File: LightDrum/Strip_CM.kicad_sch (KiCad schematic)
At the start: 26 parts, among them T701 NET-TIE, T702 NET-TIE, T703 NET-TIE, T704 NET-TIE, T705 NET-TIE, T706 NET-TIE, T707 NET-TIE, T708 NET-TIE, T709 NET-TIE, T710 NET-TIE, T711 NET-TIE, T712 NET-TIE, T713 NET-TIE, T714 NET-TIE, T715 NET-TIE, T716 NET-TIE, U701 INA4181 A2, U702 INA4181 A2

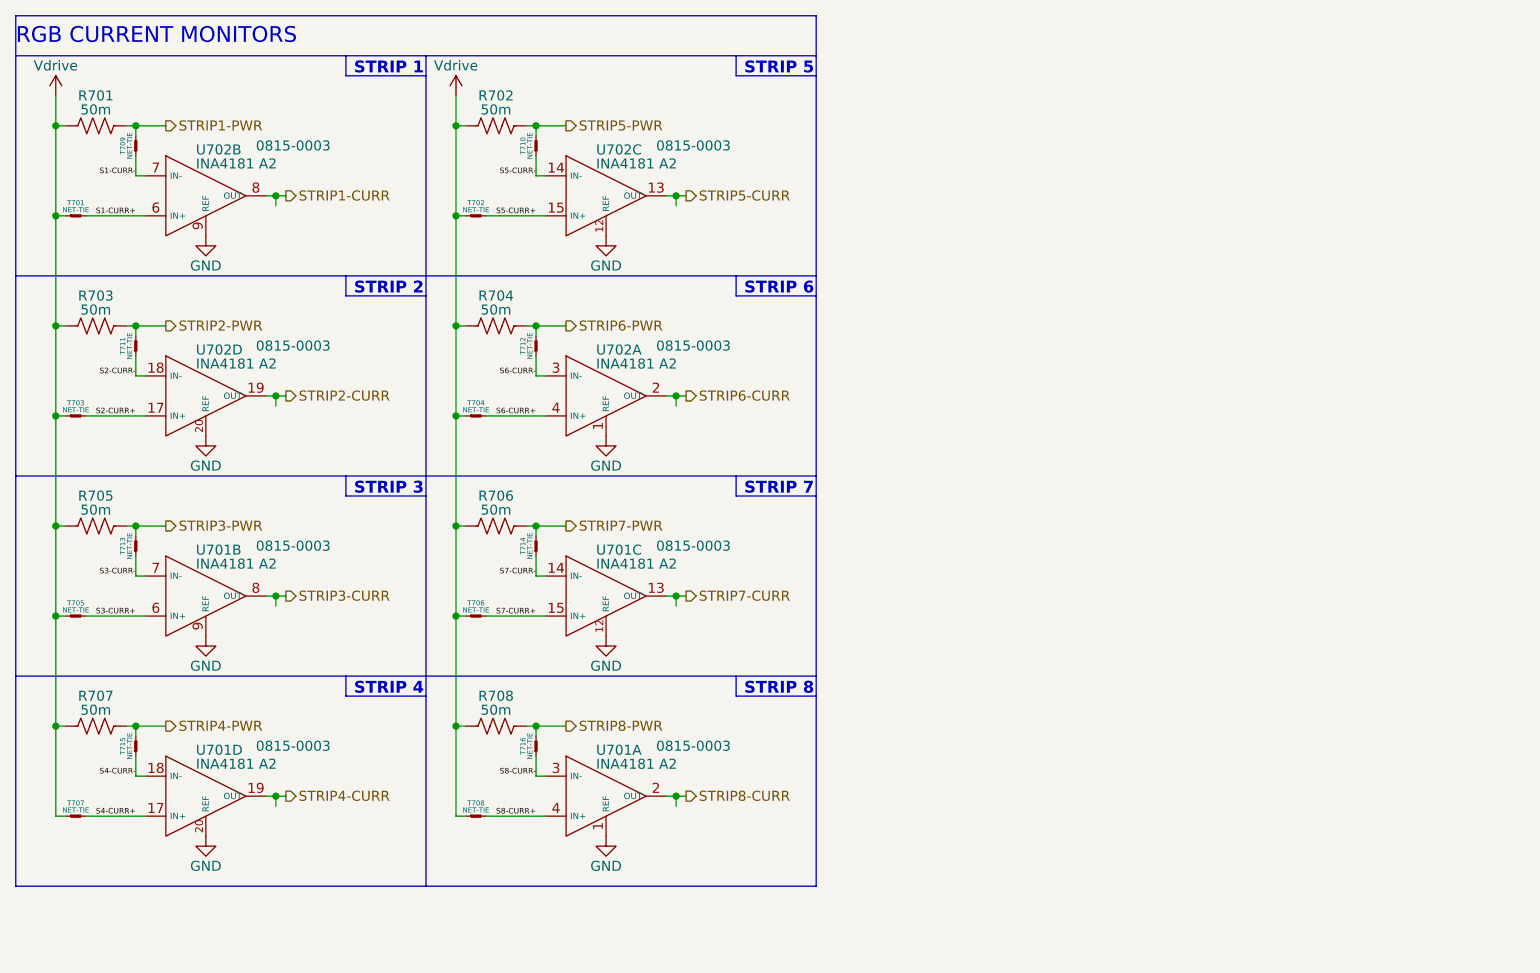
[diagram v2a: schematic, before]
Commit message: Component placement complete
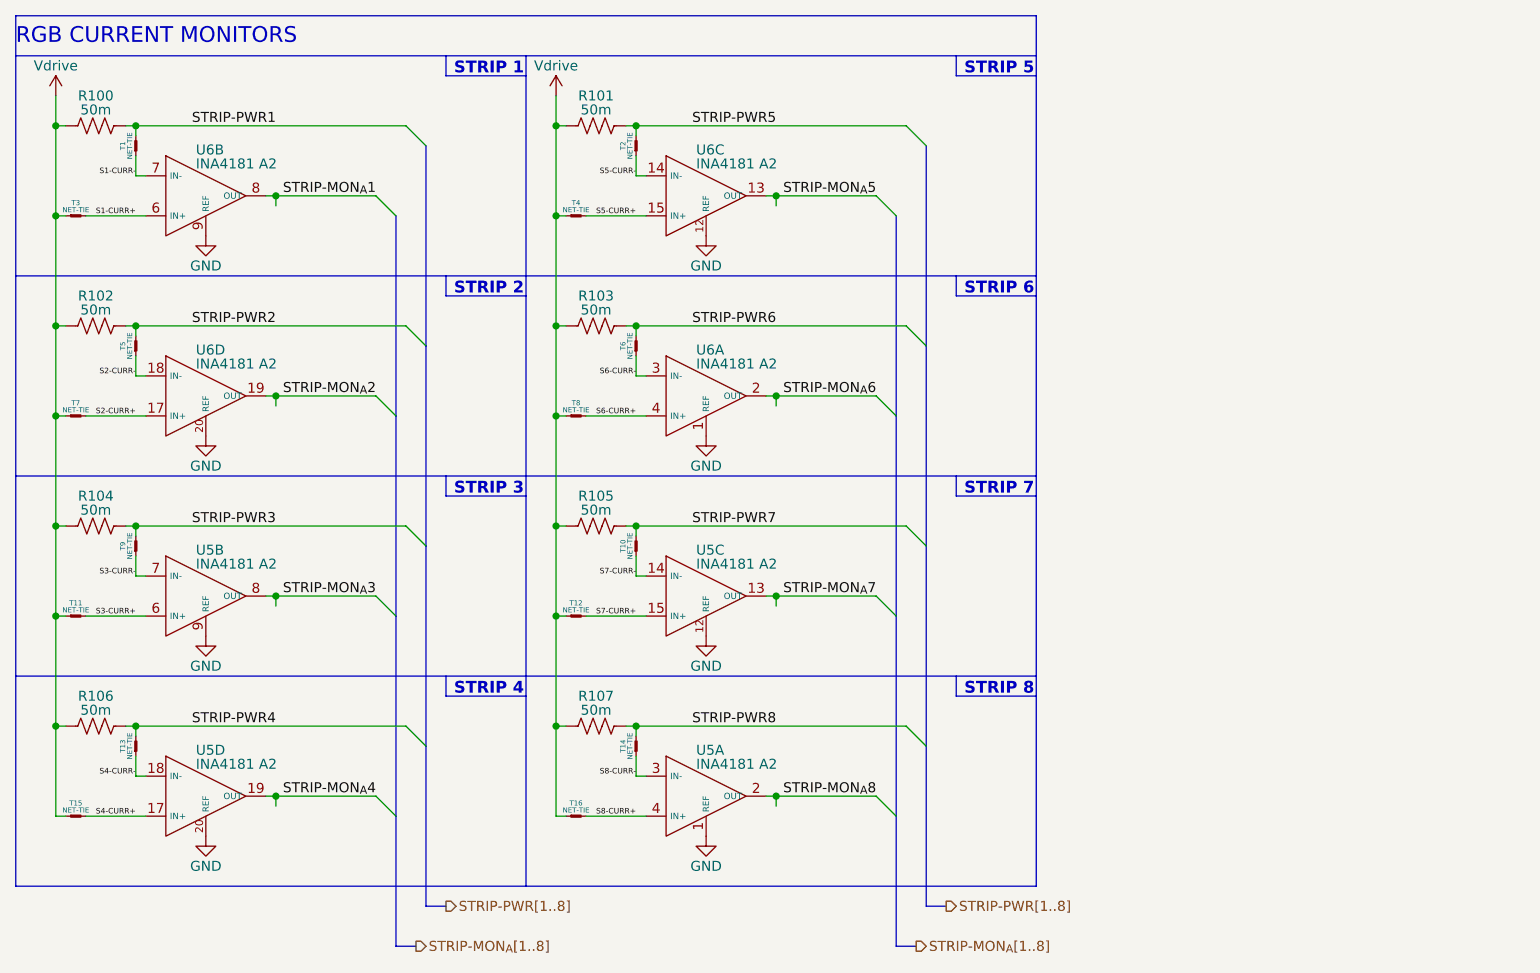
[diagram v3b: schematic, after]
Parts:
- renumbered R701 to R100, R702 to R101, R703 to R102, R704 to R103, R705 to R104, R706 to R105, R707 to R106, R708 to R107, T709 to T1, T714 to T10, T705 to T11, T706 to T12, T715 to T13, T716 to T14, T707 to T15, T708 to T16, T710 to T2, T701 to T3, T702 to T4, T711 to T5, T712 to T6, T703 to T7, T704 to T8, T713 to T9, U701 to U5, U702 to U6
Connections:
- net STRIP1-CURR renamed STRIP-MON_{A}1
- net STRIP1-PWR renamed STRIP-PWR1
- net STRIP2-CURR renamed STRIP-MON_{A}2
- net STRIP2-PWR renamed STRIP-PWR2
- net STRIP3-CURR renamed STRIP-MON_{A}3
- net STRIP3-PWR renamed STRIP-PWR3
- net STRIP4-CURR renamed STRIP-MON_{A}4
- net STRIP4-PWR renamed STRIP-PWR4
- net STRIP5-CURR renamed STRIP-MON_{A}5
- net STRIP5-PWR renamed STRIP-PWR5
- net STRIP6-CURR renamed STRIP-MON_{A}6
- net STRIP6-PWR renamed STRIP-PWR6
- net STRIP7-CURR renamed STRIP-MON_{A}7
- net STRIP7-PWR renamed STRIP-PWR7
- net STRIP8-CURR renamed STRIP-MON_{A}8
- net STRIP8-PWR renamed STRIP-PWR8
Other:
- moved on the sheet: R101, R103, R105, R107, T10, T12, T14, T16, T2, T4, T6, T8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

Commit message: First draft layout almost complete
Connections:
- net S1-CURR+: now also U6.15 (IN+); no longer U6.6 (IN+)
- net S1-CURR-: now also U6.14 (IN-); no longer U6.7 (IN-)
- net S2-CURR+: now also U6.4 (IN+); no longer U6.17 (IN+)
- net S2-CURR-: now also U6.3 (IN-); no longer U6.18 (IN-)
- net S3-CURR+: now also U5.15 (IN+); no longer U5.6 (IN+)
- net S3-CURR-: now also U5.14 (IN-); no longer U5.7 (IN-)
- net S4-CURR+: now also U5.4 (IN+); no longer U5.17 (IN+)
- net S4-CURR-: now also U5.3 (IN-); no longer U5.18 (IN-)
- net S5-CURR+: now also U6.17 (IN+); no longer U6.15 (IN+)
- net S5-CURR-: now also U6.18 (IN-); no longer U6.14 (IN-)
- net S6-CURR+: now also U6.6 (IN+); no longer U6.4 (IN+)
- net S6-CURR-: now also U6.7 (IN-); no longer U6.3 (IN-)
- net S7-CURR+: now also U5.17 (IN+); no longer U5.15 (IN+)
- net S7-CURR-: now also U5.18 (IN-); no longer U5.14 (IN-)
- net S8-CURR+: now also U5.6 (IN+); no longer U5.4 (IN+)
- net S8-CURR-: now also U5.7 (IN-); no longer U5.3 (IN-)
- net STRIP-MON_{A}1: now also U6.13 (OUT); no longer U6.8 (OUT)
- net STRIP-MON_{A}2: now also U6.2 (OUT); no longer U6.19 (OUT)
- net STRIP-MON_{A}3: now also U5.13 (OUT); no longer U5.8 (OUT)
- net STRIP-MON_{A}4: now also U5.2 (OUT); no longer U5.19 (OUT)
- net STRIP-MON_{A}5: now also U6.19 (OUT); no longer U6.13 (OUT)
- net STRIP-MON_{A}6: now also U6.8 (OUT); no longer U6.2 (OUT)
- net STRIP-MON_{A}7: now also U5.19 (OUT); no longer U5.13 (OUT)
- net STRIP-MON_{A}8: now also U5.8 (OUT); no longer U5.2 (OUT)
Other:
- moved on the sheet: U5A, U5B, U5C, U5D, U6A, U6B, U6C, U6D

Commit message: PCB Lock REV11
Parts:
- T1, T10, T11, T12, T13, T14, T15, T16, T2, T3, T4, T5, T6, T7, T8, T9: footprint Daxxn_Other:NetTie-2_SMD_Pad0.25mm -> Daxxn_Other:NetTie-2-SMALL_SMD_Pad0.2mm
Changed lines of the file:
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@@
       (effects (font (size 0.64 0.64)))
     )
-    (property "Footprint" "Daxxn_Other:NetTie-2_SMD_Pad0.25mm" (at 91.44 41.91 0)
+    (property "Footprint" "Daxxn_Other:NetTie-2-SMALL_SMD_Pad0.2mm" (at 91.44 41.91 0)
       (effects (font (size 1.27 1.27)) hide)
     )
@@
       (effects (font (size 0.64 0.64)))
     )
-    (property "Footprint" "Daxxn_Other:NetTie-2_SMD_Pad0.25mm" (at 15.24 88.9 0)
+    (property "Footprint" "Daxxn_Other:NetTie-2-SMALL_SMD_Pad0.2mm" (at 15.24 88.9 0)
       (effects (font (size 1.27 1.27)) hide)
     )
@@
       (effects (font (size 0.64 0.64)))
     )
-    (property "Footprint" "Daxxn_Other:NetTie-2_SMD_Pad0.25mm" (at 78.74 38.1 0)
+    (property "Footprint" "Daxxn_Other:NetTie-2-SMALL_SMD_Pad0.2mm" (at 78.74 38.1 0)
       (effects (font (size 1.27 1.27)) hide)
     )
@@
       (effects (font (size 0.64 0.64)))
     )
-    (property "Footprint" "Daxxn_Other:NetTie-2_SMD_Pad0.25mm" (at 27.94 92.71 0)
+    (property "Footprint" "Daxxn_Other:NetTie-2-SMALL_SMD_Pad0.2mm" (at 27.94 92.71 0)
       (effects (font (size 1.27 1.27)) hide)
     )
@@
       (effects (font (size 0.64 0.64)))
     )
-    (property "Footprint" "Daxxn_Other:NetTie-2_SMD_Pad0.25mm" (at 15.24 38.1 0)
+    (property "Footprint" "Daxxn_Other:NetTie-2-SMALL_SMD_Pad0.2mm" (at 15.24 38.1 0)
       (effects (font (size 1.27 1.27)) hide)
     )
@@
       (effects (font (size 0.64 0.64)))
     )
-    (property "Footprint" "Daxxn_Other:NetTie-2_SMD_Pad0.25mm" (at 78.74 88.9 0)
+    (property "Footprint" "Daxxn_Other:NetTie-2-SMALL_SMD_Pad0.2mm" (at 78.74 88.9 0)
       (effects (font (size 1.27 1.27)) hide)
     )
@@
       (effects (font (size 0.64 0.64)))
     )
-    (property "Footprint" "Daxxn_Other:NetTie-2_SMD_Pad0.25mm" (at 91.44 67.31 0)
+    (property "Footprint" "Daxxn_Other:NetTie-2-SMALL_SMD_Pad0.2mm" (at 91.44 67.31 0)
       (effects (font (size 1.27 1.27)) hide)
     )
@@
       (effects (font (size 0.64 0.64)))
     )
-    (property "Footprint" "Daxxn_Other:NetTie-2_SMD_Pad0.25mm" (at 78.74 114.3 0)
+    (property "Footprint" "Daxxn_Other:NetTie-2-SMALL_SMD_Pad0.2mm" (at 78.74 114.3 0)
       (effects (font (size 1.27 1.27)) hide)
     )
@@
       (effects (font (size 0.64 0.64)))
     )
-    (property "Footprint" "Daxxn_Other:NetTie-2_SMD_Pad0.25mm" (at 27.94 118.11 0)
+    (property "Footprint" "Daxxn_Other:NetTie-2-SMALL_SMD_Pad0.2mm" (at 27.94 118.11 0)
       (effects (font (size 1.27 1.27)) hide)
     )
@@
       (effects (font (size 0.64 0.64)))
     )
-    (property "Footprint" "Daxxn_Other:NetTie-2_SMD_Pad0.25mm" (at 91.44 92.71 0)
+    (property "Footprint" "Daxxn_Other:NetTie-2-SMALL_SMD_Pad0.2mm" (at 91.44 92.71 0)
       (effects (font (size 1.27 1.27)) hide)
     )
@@
       (effects (font (size 0.64 0.64)))
     )
-    (property "Footprint" "Daxxn_Other:NetTie-2_SMD_Pad0.25mm" (at 78.74 63.5 0)
+    (property "Footprint" "Daxxn_Other:NetTie-2-SMALL_SMD_Pad0.2mm" (at 78.74 63.5 0)
       (effects (font (size 1.27 1.27)) hide)
     )
@@
       (effects (font (size 0.64 0.64)))
     )
-    (property "Footprint" "Daxxn_Other:NetTie-2_SMD_Pad0.25mm" (at 27.94 41.91 0)
+    (property "Footprint" "Daxxn_Other:NetTie-2-SMALL_SMD_Pad0.2mm" (at 27.94 41.91 0)
       (effects (font (size 1.27 1.27)) hide)
     )
@@
       (effects (font (size 0.64 0.64)))
     )
-    (property "Footprint" "Daxxn_Other:NetTie-2_SMD_Pad0.25mm" (at 91.44 118.11 0)
+    (property "Footprint" "Daxxn_Other:NetTie-2-SMALL_SMD_Pad0.2mm" (at 91.44 118.11 0)
       (effects (font (size 1.27 1.27)) hide)
     )
@@
       (effects (font (size 0.64 0.64)))
     )
-    (property "Footprint" "Daxxn_Other:NetTie-2_SMD_Pad0.25mm" (at 15.24 114.3 0)
+    (property "Footprint" "Daxxn_Other:NetTie-2-SMALL_SMD_Pad0.2mm" (at 15.24 114.3 0)
       (effects (font (size 1.27 1.27)) hide)
     )
@@
       (effects (font (size 0.64 0.64)))
     )
-    (property "Footprint" "Daxxn_Other:NetTie-2_SMD_Pad0.25mm" (at 27.94 67.31 0)
+    (property "Footprint" "Daxxn_Other:NetTie-2-SMALL_SMD_Pad0.2mm" (at 27.94 67.31 0)
       (effects (font (size 1.27 1.27)) hide)
     )
@@
       (effects (font (size 0.64 0.64)))
     )
-    (property "Footprint" "Daxxn_Other:NetTie-2_SMD_Pad0.25mm" (at 15.24 63.5 0)
-      (effects (font (size 1.27 1.27)) hide)
-    )
+    (property "Footprint" "Daxxn_Other:NetTie-2-SMALL_SMD_Pad0.2mm" (at 15.24 63.5 0)
+      (effects (font (size 1.27 1.27)) hide)
+    )

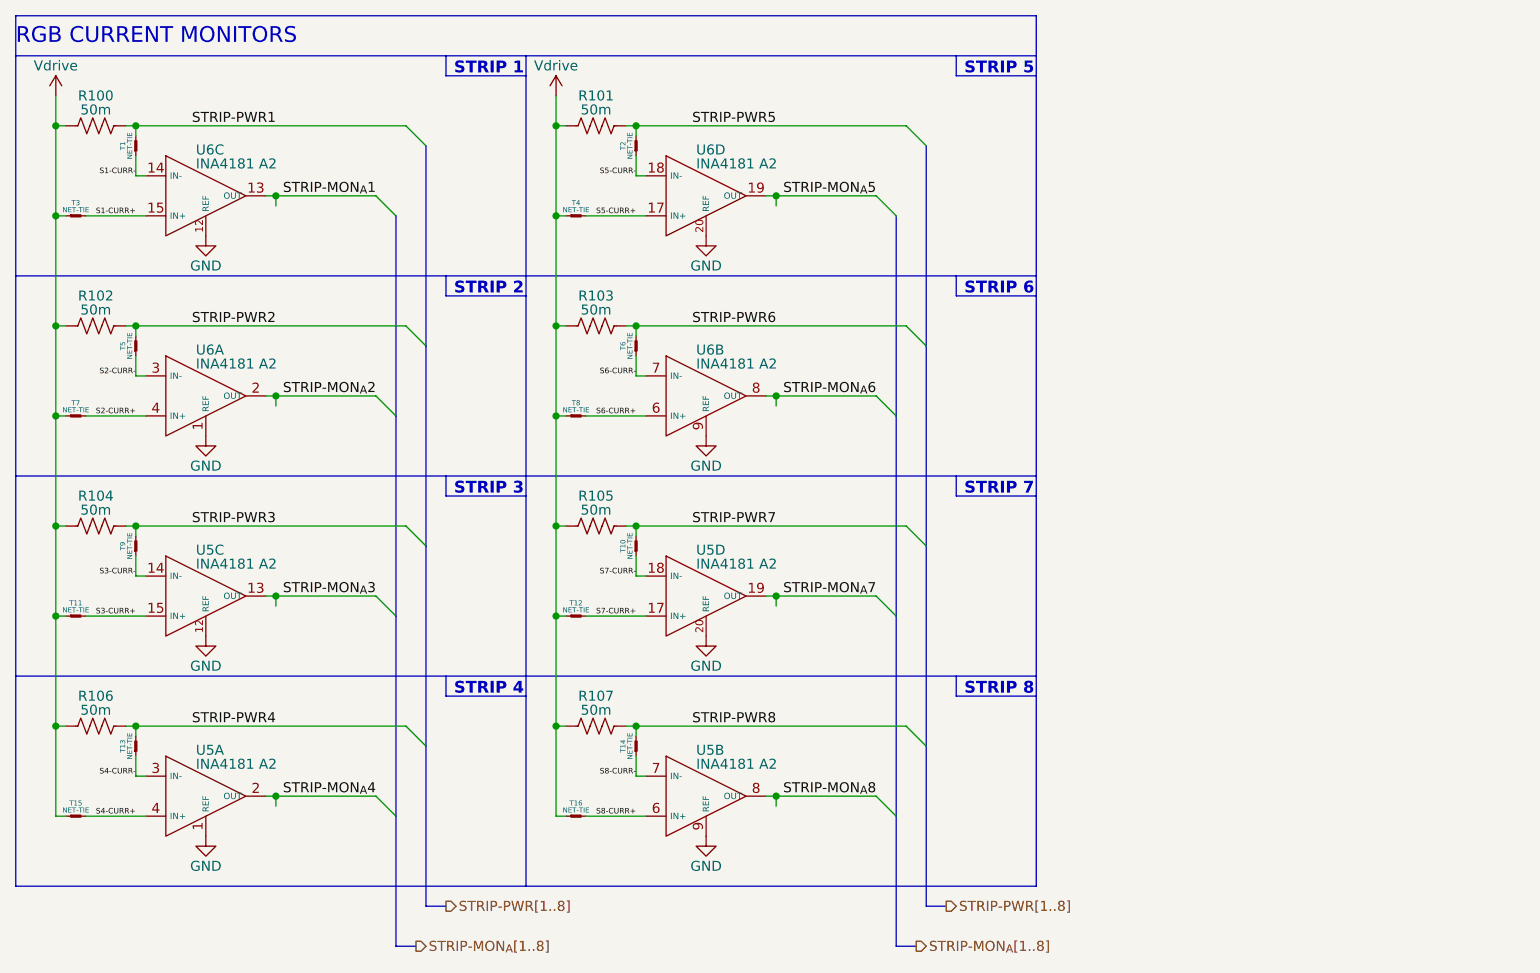
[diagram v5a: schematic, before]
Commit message: Replace DSub with much better ECU conn
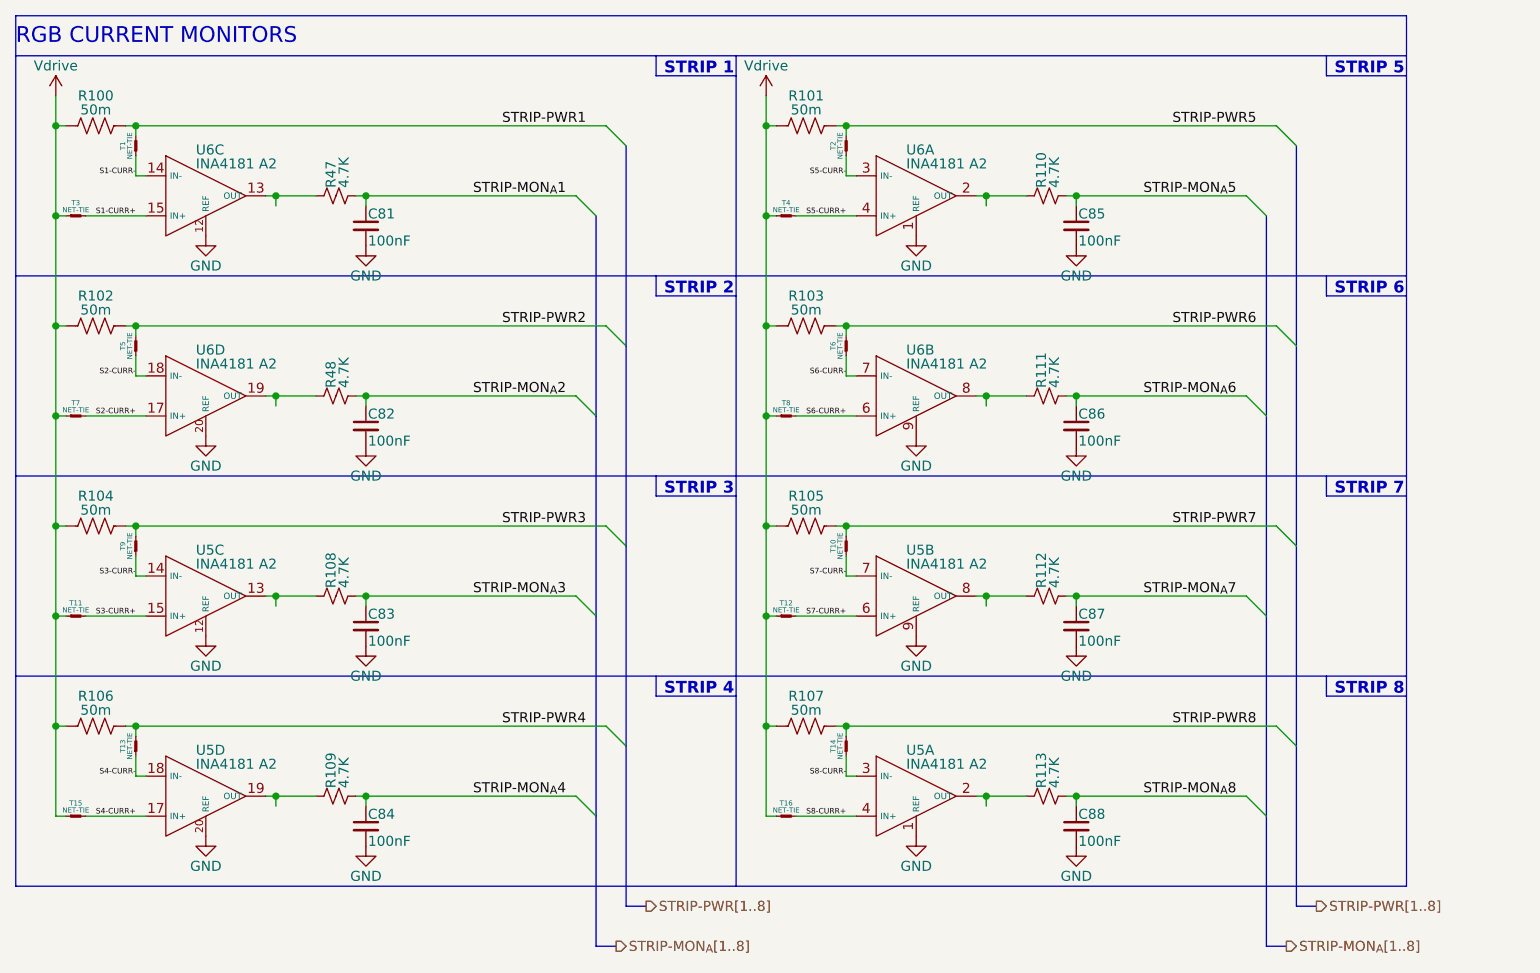
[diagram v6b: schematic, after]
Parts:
- added C81, C82, C83, C84, C85, C86, C87, C88: 100nF, Capacitor_SMD:C_0402_1005Metric, symbol Daxxn_Device:C
- added R108, R109, R110, R111, R112, R113, R47, R48: 4.7K, Resistor_SMD:R_0402_1005Metric, symbol Daxxn_Device:R
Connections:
- net GND: now also C81.2, C82.2, C83.2, C84.2, C85.2, C86.2, C87.2, C88.2
- net S2-CURR+: now also U6.17 (IN+); no longer U6.4 (IN+)
- net S2-CURR-: now also U6.18 (IN-); no longer U6.3 (IN-)
- net S4-CURR+: now also U5.17 (IN+); no longer U5.4 (IN+)
- net S4-CURR-: now also U5.18 (IN-); no longer U5.3 (IN-)
- net S5-CURR+: now also U6.4 (IN+); no longer U6.17 (IN+)
- net S5-CURR-: now also U6.3 (IN-); no longer U6.18 (IN-)
- net S7-CURR+: now also U5.6 (IN+); no longer U5.17 (IN+)
- net S7-CURR-: now also U5.7 (IN-); no longer U5.18 (IN-)
- net S8-CURR+: now also U5.4 (IN+); no longer U5.6 (IN+)
- net S8-CURR-: now also U5.3 (IN-); no longer U5.7 (IN-)
- net STRIP-MON_{A}1: now also C81.1, R47.2; no longer U6.13 (OUT)
- net STRIP-MON_{A}2: now also C82.1, R48.2; no longer U6.2 (OUT)
- net STRIP-MON_{A}3: now also C83.1, R108.2; no longer U5.13 (OUT)
- net STRIP-MON_{A}4: now also C84.1, R109.2; no longer U5.2 (OUT)
- net STRIP-MON_{A}5: now also C85.1, R110.2; no longer U6.19 (OUT)
- net STRIP-MON_{A}6: now also C86.1, R111.2; no longer U6.8 (OUT)
- net STRIP-MON_{A}7: now also C87.1, R112.2; no longer U5.19 (OUT)
- net STRIP-MON_{A}8: now also C88.1, R113.2; no longer U5.8 (OUT)
- new net: R113.1, U5.2 (OUT)
- new net: R108.1, U5.13 (OUT)
- new net: R47.1, U6.13 (OUT)
- new net: R111.1, U6.8 (OUT)
- new net: R110.1, U6.2 (OUT)
- new net: R109.1, U5.19 (OUT)
- new net: R48.1, U6.19 (OUT)
- new net: R112.1, U5.8 (OUT)
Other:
- moved on the sheet: R101, R103, R105, R107, T10, T12, T14, T16, T2, T4, T6, T8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
